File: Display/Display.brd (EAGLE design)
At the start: 36.3 x 29.8 mm, 29 parts, among them SW1 SWITCH-PTS-810, SW2 SWITCH-PTS-810, SW3 SWITCH-PTS-810, U1 ER-OLED0.95-2C, U2 FAN5331SX, U3 ATSAMD20E17A-AU, U4 MIC5205-3.3YM5 TR

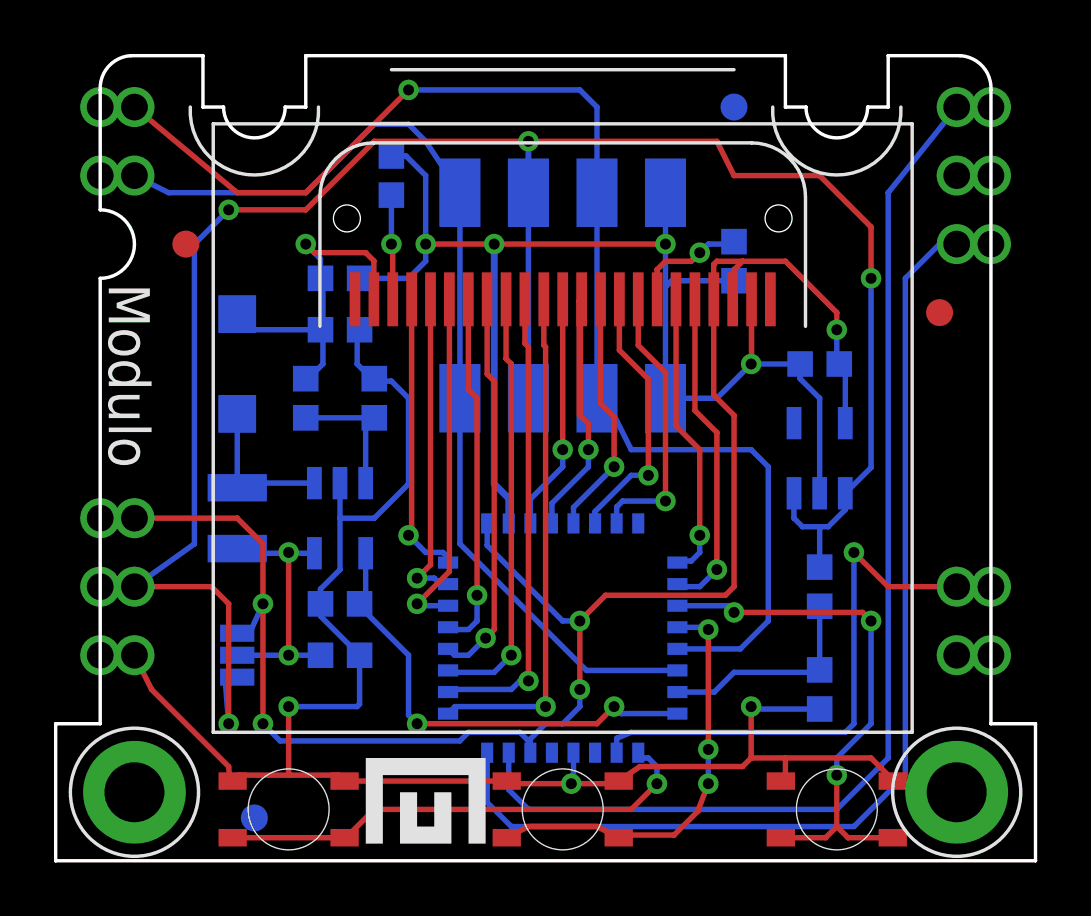
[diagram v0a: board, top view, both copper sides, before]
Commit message: New diode selections
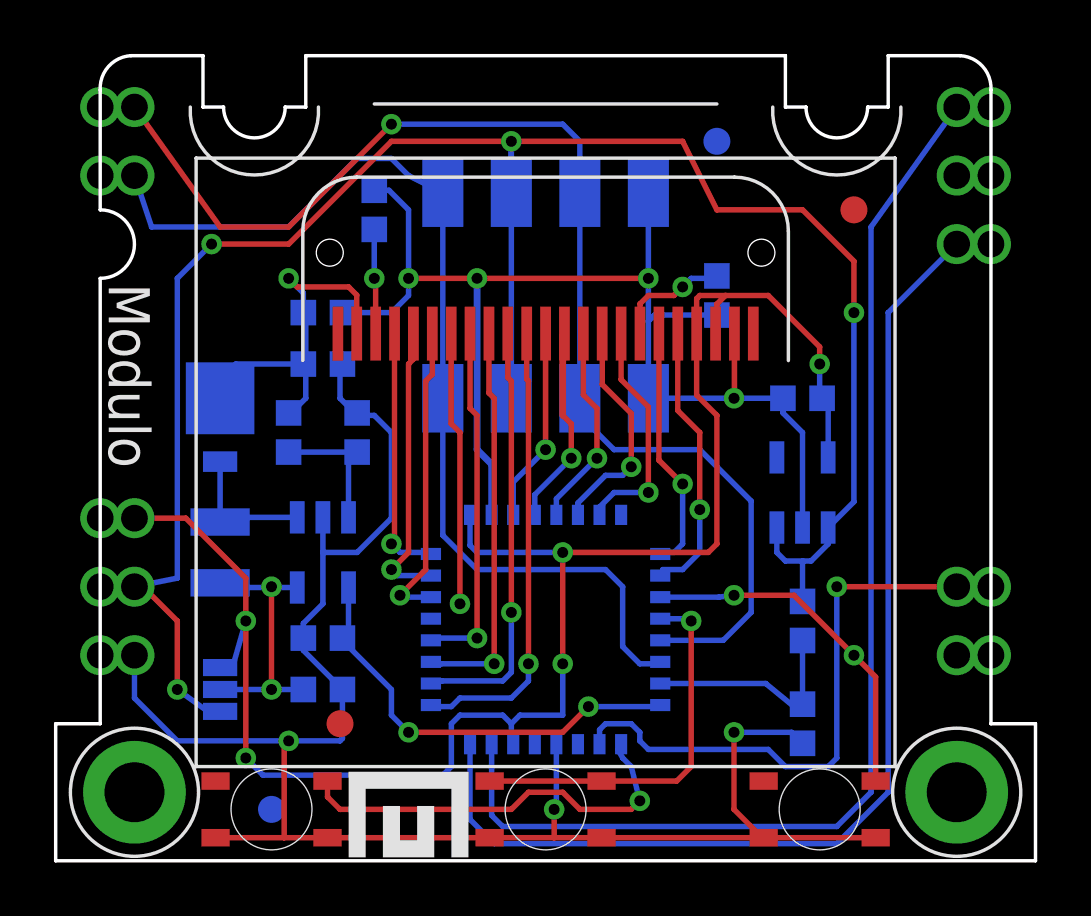
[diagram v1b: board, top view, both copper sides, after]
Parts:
- D1: device microbuilder:SOD-123 -> Modulo:SMP
- moved U$2 27.0 mm to (27.6, 22.9)
- moved F1 18.7 mm to (10.2, 5.08)
- moved F2 4.96 mm to (29.2, 24.1)
- moved R2 1.42 mm to (24.1, 21.0)
- moved C1 1.42 mm to (9.53, 6.35)
- moved JP1 1.42 mm to (5.71, 6.35)
- moved C5 1.42 mm to (27.3, 17.1)
- moved F3 1.42 mm to (24.1, 26.7)
- moved R5 1.42 mm to (27.3, 8.89)
- moved R6 1.42 mm to (27.3, 5.08)
- moved U4 1.42 mm to (27.3, 13.7)
- moved C2 1.42 mm to (11.4, 24.1)
- moved C3 1.42 mm to (9.53, 18.4)
- moved C4 1.42 mm to (9.53, 20.3)
- moved D1 1.42 mm to (5.71, 17.1)
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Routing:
- net BUTTON3: track 20.1 -> 13.1 mm, vias 3 -> 2
- net +5V: track 79.5 -> 75.8 mm
- net GND: track 114.7 -> 118.3 mm
- net D4: track 13.3 -> 10.2 mm
- net SDA: track 49.3 -> 46.4 mm
- net BUTTON1: track 18.1 -> 15.4 mm
- net SWCLK: track 41.5 -> 43.8 mm
- net D0: track 18.8 -> 16.9 mm
- net BS1: track 12.1 -> 10.3 mm
- net CS: track 10.4 -> 8.63 mm
- net D1: track 17.3 -> 15.7 mm
- net DISPLAY_RESET: track 9.94 -> 8.35 mm
- net D5: track 13.0 -> 11.4 mm
- net BS0: track 10.7 -> 9.14 mm
- net D/C: track 9.14 -> 7.55 mm
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
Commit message: Fixed a missing connection.
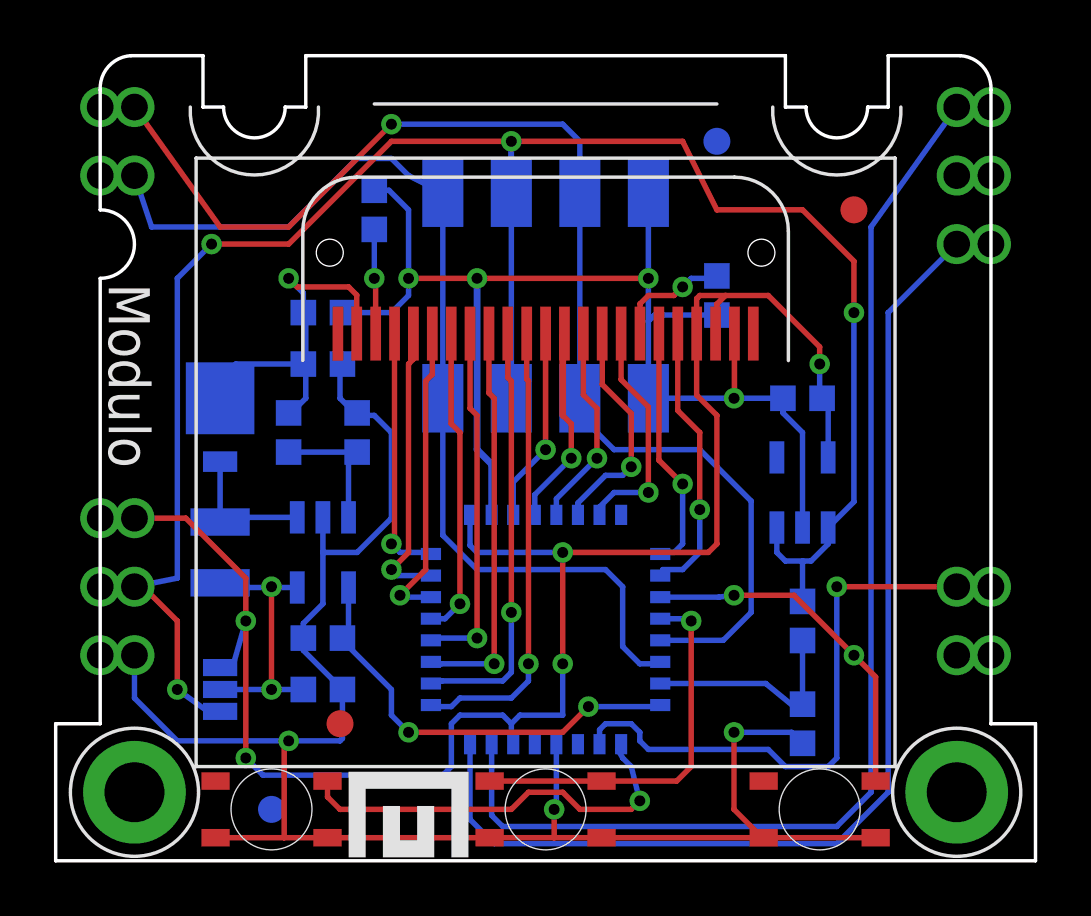
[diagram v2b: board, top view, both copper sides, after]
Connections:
- net BS0 renamed BS2
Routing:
- net D4: track 10.2 -> 11.5 mm

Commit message: Check point of current PCB designs. Among other things I think this change includes rewiring of programming lines on many of the boards,.
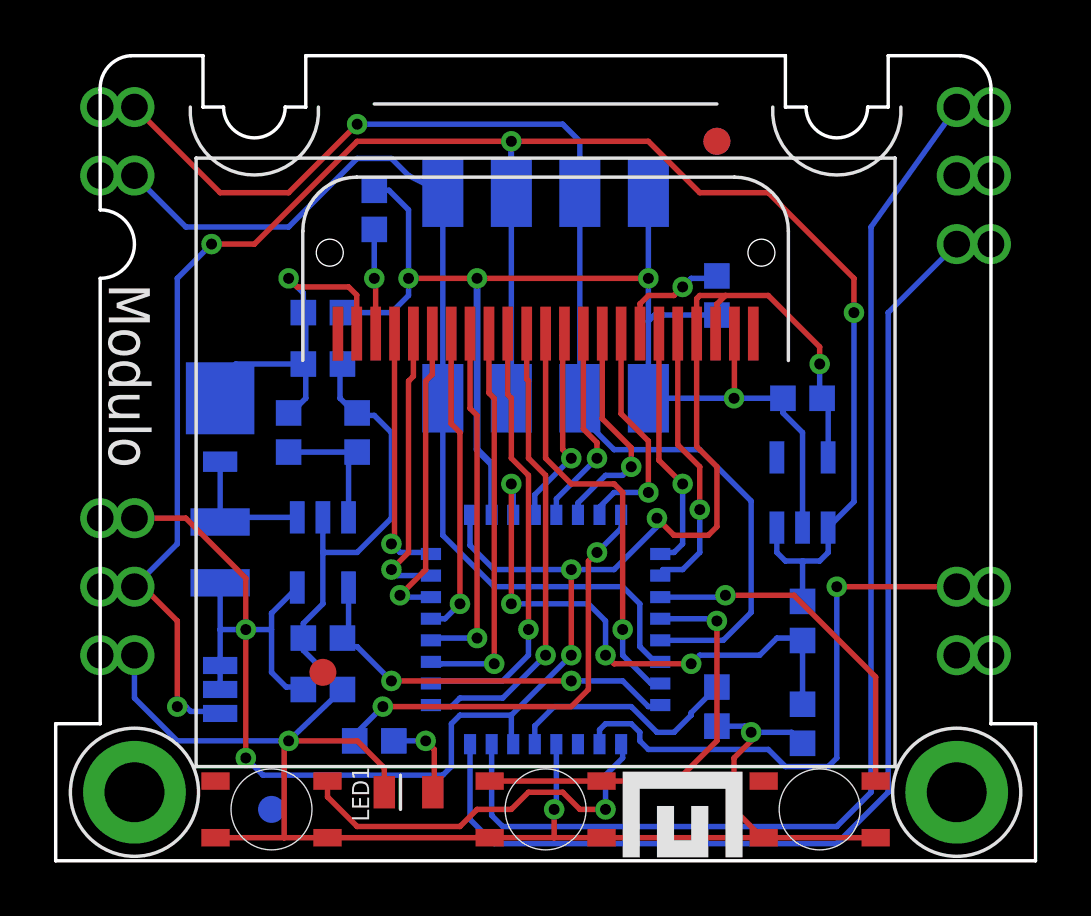
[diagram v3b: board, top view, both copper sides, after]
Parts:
- added C6: .1uF, Modulo:0603
- added LED1: blue, Modulo:0805-LED
- added R7: 1KΩ, Modulo:0603
- JP1: value JUMPER-31-2 -> (none); device SparkFun-Passives:SJ_3_PASTE1&2 -> SparkFun-Passives:SJ_3
- moved U$1 10.2 mm to (22.5, 0.76)
- moved F2 5.68 mm to (24.1, 26.7)
- moved U$2 2.13 mm to (29.5, 21.9), turned to 0 degrees
- moved F1 2.01 mm to (9.53, 6.99)
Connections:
- removed net VIN: C1.1, JP1.2, L1.P$1, U2.5
- new net LED: R7.2, U3.16
- new net N$4: C6.1, U3.29
- new net N$6: LED1.A, R7.1
- net +3.3V: now also C1.1, JP1.2, L1.P$1, U2.5
- net GND: now also C6.2, LED1.C
- net RD: now also U3.23; no longer U3.11
- net VSENSE: now also U3.11; no longer U3.23
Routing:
- net LED: track 0.00 -> 16.6 mm, vias 0 -> 2
- net VSENSE: track 7.98 -> 21.0 mm, vias 0 -> 4
- net VIN: track 10.1 -> 0.00 mm, vias 2 -> 0
- net N$4: track 0.00 -> 8.86 mm
- net RD: track 7.22 -> 15.9 mm
- net +3.3V: track 66.1 -> 74.6 mm, vias 5 -> 6
- net GND: track 118.3 -> 123.1 mm
- net N$6: track 0.00 -> 3.24 mm, vias 0 -> 1
- net SDA: track 46.4 -> 44.9 mm
- net SHDN: track 16.4 -> 15.0 mm
- net BUTTON2: track 14.3 -> 15.6 mm
- net SCL: track 38.3 -> 37.4 mm
- net +5V: track 75.8 -> 74.9 mm
- net D1: track 15.7 -> 16.3 mm
- net BUTTON3: vias 2 -> 1

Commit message: Various fixes
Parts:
- R1: value 10KΩ -> 10K
- moved R7 0.95 mm to (10.5, 4.45)
- moved C6 0.45 mm to (24.4, 6.03), turned to 180 degrees
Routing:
- net SWCLK: track 43.8 -> 26.1 mm, vias 0 -> 1
- net RESET: track 21.2 -> 30.4 mm, vias 1 -> 2
- net +5V: track 74.9 -> 80.5 mm, vias 4 -> 3
- net +3.3V: track 74.6 -> 79.2 mm
- net BUTTON3: track 13.1 -> 17.3 mm
- net GND: track 123.1 -> 124.7 mm
- net LED: track 16.6 -> 17.5 mm
- net N$4: track 8.86 -> 8.21 mm
- net SCL: track 37.4 -> 36.8 mm
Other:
- outline, holes or cut-outs redrawn

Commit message: Added unique board prefixes to part numbers due to CM requirements
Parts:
- removed F2, F3: FIDUCIAL, Modulo:FIDUCIAL_1MM
- added 9-F2, 9-F3: FIDUCIAL, Modulo:FIDUCIAL_1MM
- 9-R1: value 10K -> 10KΩ
- 9-U4: value MIC5205-3.3YM5 TR -> VREG-MIC5205-3.3V
- renumbered C1 to 9-C1, C2 to 9-C2, C3 to 9-C3, C4 to 9-C4, C5 to 9-C5, C6 to 9-C6, D1 to 9-D1, F1 to 9-F1, F4 to 9-F4, JP1 to 9-JP1, JP2 to 9-JP2, L1 to 9-L1, LED1 to 9-LED1, PCB1 to 9-PCB1, R1 to 9-R1, R2 to 9-R2, R3 to 9-R3, R4 to 9-R4, R5 to 9-R5, R6 to 9-R6, R7 to 9-R7, SW1 to 9-SW1, SW2 to 9-SW2, SW3 to 9-SW3, U1 to 9-U1, U2 to 9-U2, U3 to 9-U3, U4 to 9-U4
